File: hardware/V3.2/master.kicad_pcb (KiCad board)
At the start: 4 copper layers, 40 x 40 mm, 129 parts, among them J1 USB-C, J2 DRILL, J3 DRILL, J4 DRILL, J5 DRILL, J6 STACK-UP-HIGH, J7 STACK-HIGH, J8 STACK-UP-LOW, J9 STACK-DOWN, P1 Port A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

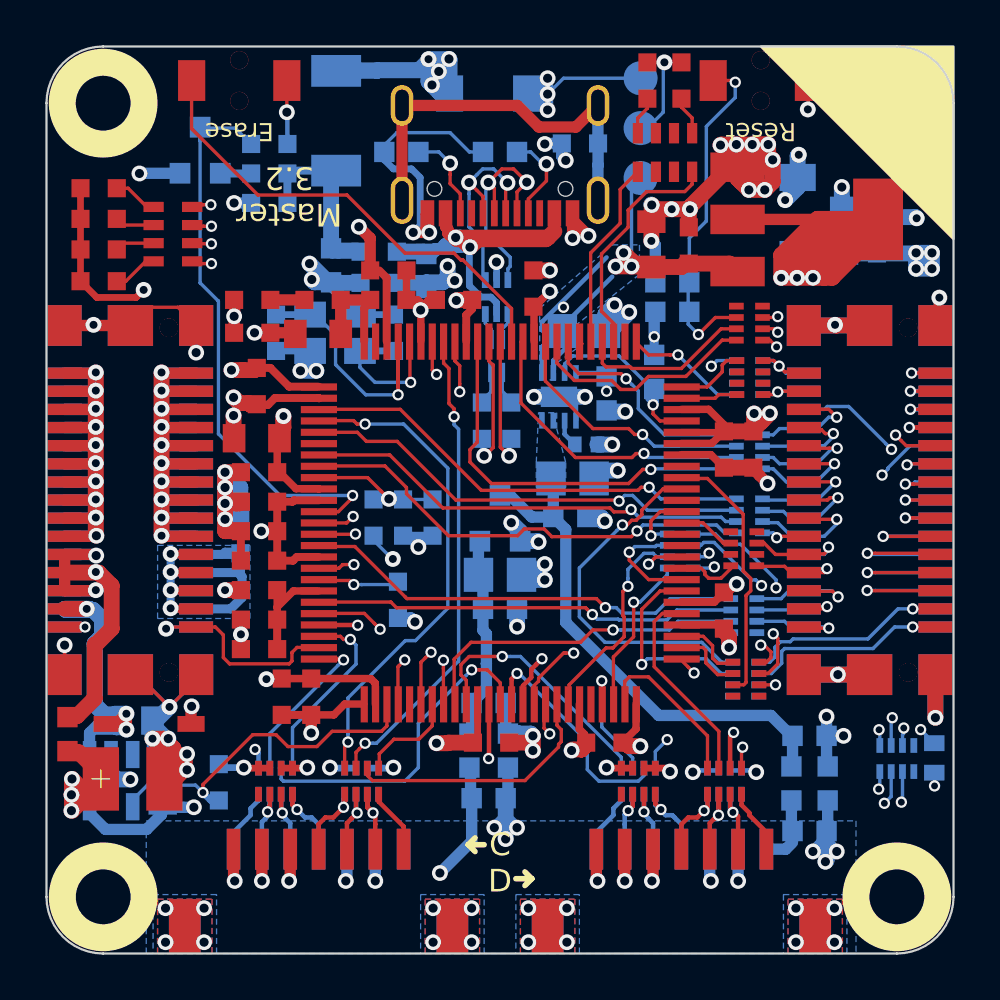
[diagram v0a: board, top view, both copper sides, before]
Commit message: add fiducials and logos
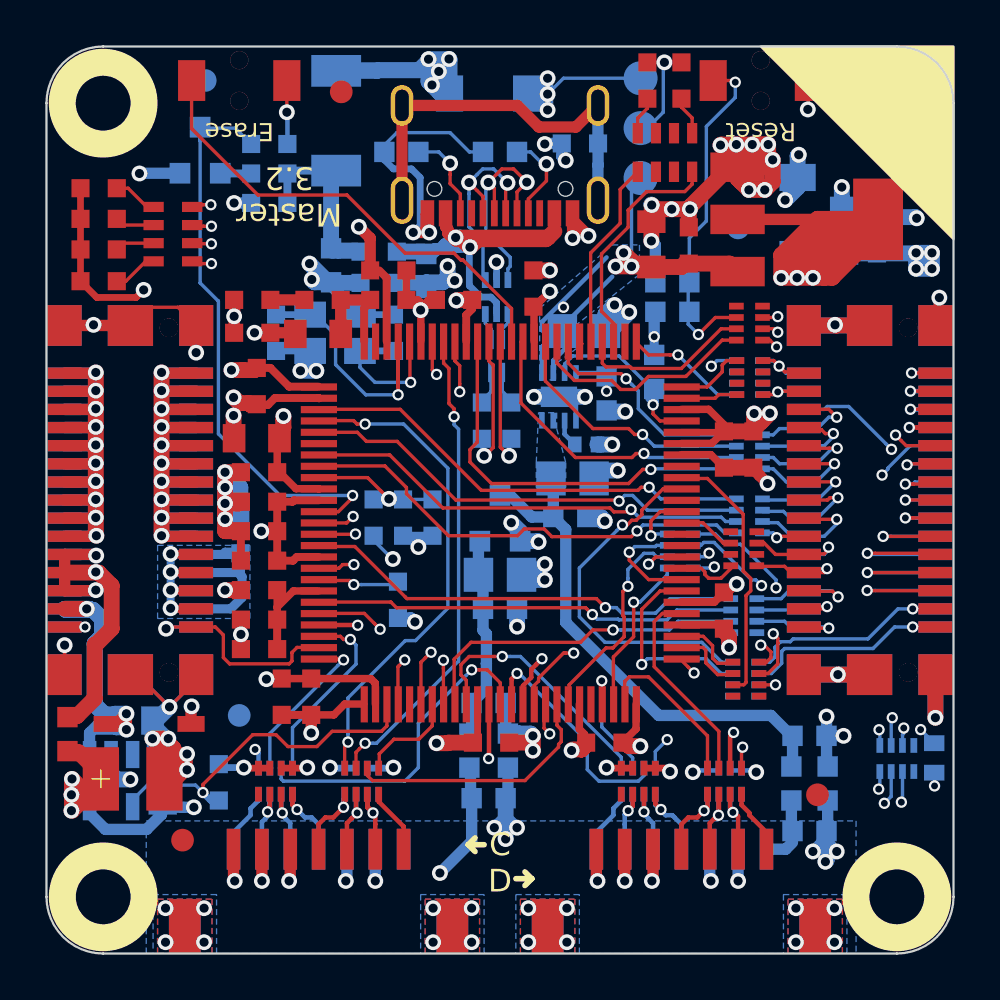
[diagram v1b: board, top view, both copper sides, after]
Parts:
- added Fiducial_Mark: VAL**, kicad-libraries:Fiducial_Mark, F.Cu at (131.0, 105.0)
- added Fiducial_Mark: VAL**, kicad-libraries:Fiducial_Mark, F.Cu at (138.0, 72.0)
- added Fiducial_Mark: VAL**, kicad-libraries:Fiducial_Mark, F.Cu at (159.0, 103.0)
- added Fiducial_Mark: VAL**, kicad-libraries:Fiducial_Mark, B.Cu at (155.5, 78.0)
- added Fiducial_Mark: VAL**, kicad-libraries:Fiducial_Mark, B.Cu at (133.5, 99.5)
- added Fiducial_Mark: VAL**, kicad-libraries:Fiducial_Mark, B.Cu at (132.0, 71.5)
- added G***: LOGO, kicad-libraries:Logo_31x31, B.Cu at (129.9, 78.0)
- added VAL: WEEE_7mm, kicad-libraries:WEEE_7mm, B.Cu at (149.8, 97.0)
- added VAL: CE_5mm, kicad-libraries:CE_5mm, B.Cu at (137.3, 97.0)
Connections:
- net STACK-HIGH/JTAG-TMS renamed STACK-HIGH/JTAG-TMS
- net STACK-I2C-SCL/JTAG-TDO renamed STACK-I2C-SCL/JTAG-TDO
- net STACK-I2C-SDA/JTAG-TDI renamed STACK-I2C-SDA/JTAG-TDI
- net STACK-SYNC/JTAG-TCK renamed STACK-SYNC/JTAG-TCK
- CP1 pad 1: Net-(CP1-Pad1) -> unconnected-(CP1-Pad1)
- CP2 pad 1: Net-(CP2-Pad1) -> unconnected-(CP2-Pad1)
- CP3 pad 1: Net-(CP3-Pad1) -> unconnected-(CP3-Pad1)
- CP4 pad 1: Net-(CP4-Pad1) -> unconnected-(CP4-Pad1)
- RP3 pad 2: Net-(RP3-Pad2) -> unconnected-(RP3-Pad2)
- RP3 pad 3: Net-(RP3-Pad3) -> unconnected-(RP3-Pad3)
- RP3 pad 6: Net-(RP3-Pad6) -> unconnected-(RP3-Pad6)
- RP3 pad 7: Net-(RP3-Pad7) -> unconnected-(RP3-Pad7)
- RP303 pad 1: Net-(RP303-Pad1) -> unconnected-(RP303-Pad1)
- RP303 pad 3: Net-(RP303-Pad3) -> unconnected-(RP303-Pad3)
- RP303 pad 6: Net-(RP303-Pad6) -> unconnected-(RP303-Pad6)
- RP303 pad 8: Net-(RP303-Pad8) -> unconnected-(RP303-Pad8)
- RP304 pad 1: Net-(RP304-Pad1) -> unconnected-(RP304-Pad1)
- RP304 pad 8: Net-(RP304-Pad8) -> unconnected-(RP304-Pad8)
- RP305 pad 1: Net-(RP305-Pad1) -> unconnected-(RP305-Pad1)
- RP305 pad 8: Net-(RP305-Pad8) -> unconnected-(RP305-Pad8)
- RP306 pad 4: Net-(RP306-Pad4) -> unconnected-(RP306-Pad4)
- RP306 pad 5: Net-(RP306-Pad5) -> unconnected-(RP306-Pad5)
- RP308 pad 3: Net-(RP308-Pad3) -> unconnected-(RP308-Pad3)
- RP308 pad 4: Net-(RP308-Pad4) -> unconnected-(RP308-Pad4)
- RP308 pad 5: Net-(RP308-Pad5) -> unconnected-(RP308-Pad5)
- RP308 pad 6: Net-(RP308-Pad6) -> unconnected-(RP308-Pad6)
- RP309 pad 1: Net-(RP309-Pad1) -> unconnected-(RP309-Pad1)
- RP309 pad 8: Net-(RP309-Pad8) -> unconnected-(RP309-Pad8)
- RP310 pad 2: Net-(RP310-Pad2) -> unconnected-(RP310-Pad2)
- RP310 pad 3: Net-(RP310-Pad3) -> unconnected-(RP310-Pad3)
- RP310 pad 6: Net-(RP310-Pad6) -> unconnected-(RP310-Pad6)
- RP310 pad 7: Net-(RP310-Pad7) -> unconnected-(RP310-Pad7)
- RP8 pad 2: Net-(RP8-Pad2) -> unconnected-(RP8-Pad2)
- RP8 pad 3: Net-(RP8-Pad3) -> unconnected-(RP8-Pad3)
- RP8 pad 6: Net-(RP8-Pad6) -> unconnected-(RP8-Pad6)
- RP8 pad 7: Net-(RP8-Pad7) -> unconnected-(RP8-Pad7)
- U1 pad 30: Net-(U1-Pad30) -> unconnected-(U1-Pad30)
- U1 pad 46: Net-(U1-Pad46) -> unconnected-(U1-Pad46)
- U1 pad 6: Net-(U1-Pad6) -> unconnected-(U1-Pad6)
- U1 pad 61: Net-(U1-Pad61) -> unconnected-(U1-Pad61)
- U1 pad 62: Net-(U1-Pad62) -> unconnected-(U1-Pad62)
- U1 pad 65: Net-(U1-Pad65) -> unconnected-(U1-Pad65)
- U1 pad 68: Net-(U1-Pad68) -> unconnected-(U1-Pad68)
- U1 pad 77: Net-(U1-Pad77) -> unconnected-(U1-Pad77)
- U1 pad 81: Net-(U1-Pad81) -> unconnected-(U1-Pad81)
- U1 pad 99: Net-(U1-Pad99) -> unconnected-(U1-Pad99)
- U13 pad 3: Net-(U13-Pad3) -> unconnected-(U13-Pad3)
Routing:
- added copper zone on In2.Cu, net 3,3VBricklet
- added copper zone on In2.Cu, net 3V3
- added copper zone on In1.Cu, net GND
- added copper zone on In1.Cu, net GNDD1
- removed copper zone on VCC, net 3,3VBricklet
- removed copper zone on VCC, net 3V3
- removed copper zone on GND, net GND
- removed copper zone on GND, net GNDD1
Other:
- net class Default removed
